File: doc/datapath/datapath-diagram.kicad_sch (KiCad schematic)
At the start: 26 parts, among them U17 ip, U19 insn, U27 stack[0], U28 stack[1], U29 ……, U32 cd_timer, U4 cstack[0], U5 cstack[1], U6 ……

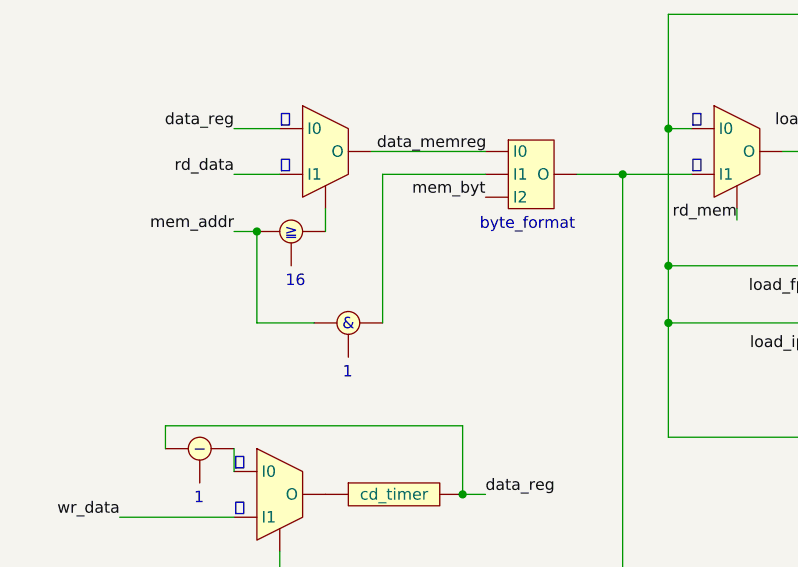
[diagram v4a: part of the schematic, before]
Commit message: CPUを新しいISAに合わせて再実装
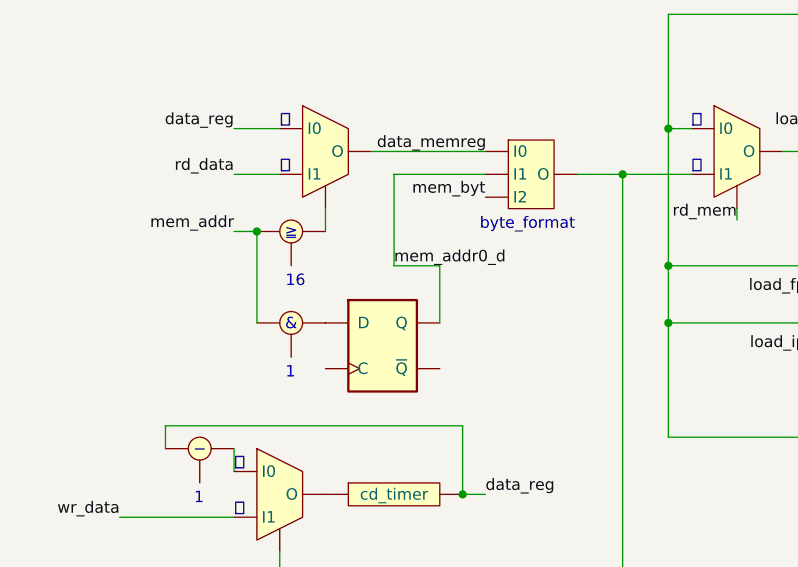
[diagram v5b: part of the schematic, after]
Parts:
- added U9: D-FF, symbol uchan:D-FF
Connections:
- net at U28.: now also U15. (O), U3. (O)
- net at U27.: now also U3. (O), U40. (O); no longer U18. (O)
- new net: U1., U31. (O)
- new net: U18. (O), U19., U34. (O)
- new net: U18. (O), U27.
- new net: U32., U36. (O)
- new net: U33., U9.~ (~{Q})
- new net: U., U40. (O)
- new net: U17., U40. (O)
- new net: U4., U40. (O)
- new net: U12. (O), U40. (O)
- new net: U36. (O), U37.
- new net: U12. (O), U2.
- new net: U15. (O), U2.
- new net: U36. (O), U39.
- new net: U38., U39.
- new net mem_addr0_d: U34. (O), U9.~ (~{Q})
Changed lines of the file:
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@@
-    (stroke (width 0) (type default))
-  )
-  (wire (pts (xy 111.76 69.85) (xy 111.76 53.34))
     (stroke (width 0) (type default))
   )
@@
     (stroke (width 0) (type default))
   )
-  (wire (pts (xy 97.79 69.85) (xy 104.14 69.85))
+  (wire (pts (xy 113.03 63.5) (xy 113.03 53.34))
     (stroke (width 0) (type default))
   )
@@
     (stroke (width 0) (type default))
   )
+  (wire (pts (xy 118.11 63.5) (xy 113.03 63.5))
+    (stroke (width 0) (type default))
+  )
   (wire (pts (xy 184.15 55.88) (xy 184.15 69.85))
     (stroke (width 0) (type default))
@@
     (stroke (width 0) (type default))
   )
+  (wire (pts (xy 118.11 69.85) (xy 118.11 63.5))
+    (stroke (width 0) (type default))
+  )
   (wire (pts (xy 186.69 58.42) (xy 193.04 58.42))
     (stroke (width 0) (type default))
@@
     (stroke (width 0) (type default))
   )
-  (wire (pts (xy 111.76 53.34) (xy 123.19 53.34))
+  (wire (pts (xy 113.03 53.34) (xy 123.19 53.34))
     (stroke (width 0) (type default))
   )
@@
   )
   (text_box "&"
-    (at 106.68 68.58 0) (size 2.54 2.54)
+    (at 100.33 68.58 0) (size 2.54 2.54)
     (stroke (width -0.0001) (type default))
     (fill (type none))
@@
     (effects (font (size 1.27 1.27)) (justify left bottom))
   )
-  (text "1" (at 107.315 76.2 0)
+  (text "1" (at 100.965 76.2 0)
     (effects (font (size 1.27 1.27)) (justify left bottom))
   )
@@
   )
   (label "load_fp" (at 191.77 124.46 0) (fields_autoplaced)
+    (effects (font (size 1.27 1.27)) (justify left bottom))
+  )
+  (label "mem_addr0_d" (at 113.03 63.5 0) (fields_autoplaced)
     (effects (font (size 1.27 1.27)) (justify left bottom))
   )
@@
     )
   )
-  (symbol (lib_id "Logic_Component:ALU_Circle_Left_Bottom") (at 107.95 69.85 0) (unit 1)
+  (symbol (lib_id "Logic_Component:ALU_Circle_Left_Bottom") (at 101.6 69.85 0) (unit 1)
     (in_bom yes) (on_board yes) (dnp no) (fields_autoplaced)
-    (property "Reference" "U33" (at 107.95 67.31 0)
-      (effects (font (size 1.27 1.27)) hide)
-    )
-    (property "Value" "~" (at 107.95 69.85 0)
-      (effects (font (size 1.27 1.27)))
-    )
-    (property "Footprint" "" (at 107.95 69.85 0)
-      (effects (font (size 1.27 1.27)) hide)
-    )
-    (property "Datasheet" "" (at 107.95 69.85 0)
+    (property "Reference" "U33" (at 101.6 67.31 0)
+      (effects (font (size 1.27 1.27)) hide)
+    )
+    (property "Value" "~" (at 101.6 69.85 0)
+      (effects (font (size 1.27 1.27)))
+    )
+    (property "Footprint" "" (at 101.6 69.85 0)
+      (effects (font (size 1.27 1.27)) hide)
+    )
+    (property "Datasheet" "" (at 101.6 69.85 0)
       (effects (font (size 1.27 1.27)) hide)
     )
@@
         )
       )
+    )
+  )
+  (symbol (lib_id "uchan:D-FF") (at 111.76 72.39 0) (unit 1)
+    (in_bom yes) (on_board yes) (dnp no) (fields_autoplaced)
+    (property "Reference" "U9" (at 111.76 66.04 0)
+      (effects (font (size 1.27 1.27)) hide)
+    )
+    (property "Value" "D-FF" (at 111.76 66.2211 0)
+      (effects (font (size 1.27 1.27)) hide)
+    )
+    (property "Footprint" "" (at 111.76 72.39 0)
+      (effects (font (size 1.27 1.27)) hide)
+    )
+    (property "Datasheet" "74xx/74hc_hct74.pdf" (at 111.76 72.39 0)
+      (effects (font (size 1.27 1.27)) hide)
+    )
+    (pin "~")
+    (pin "~")
+    (pin "~")
+    (pin "~")
+    (instances
+      (project "datapath-diagram"
+        (path "/af1fd5ae-daa0-4a17-8ab4-fe581cd231ee"
+          (reference "U9") (unit 1)
+        )
+      )

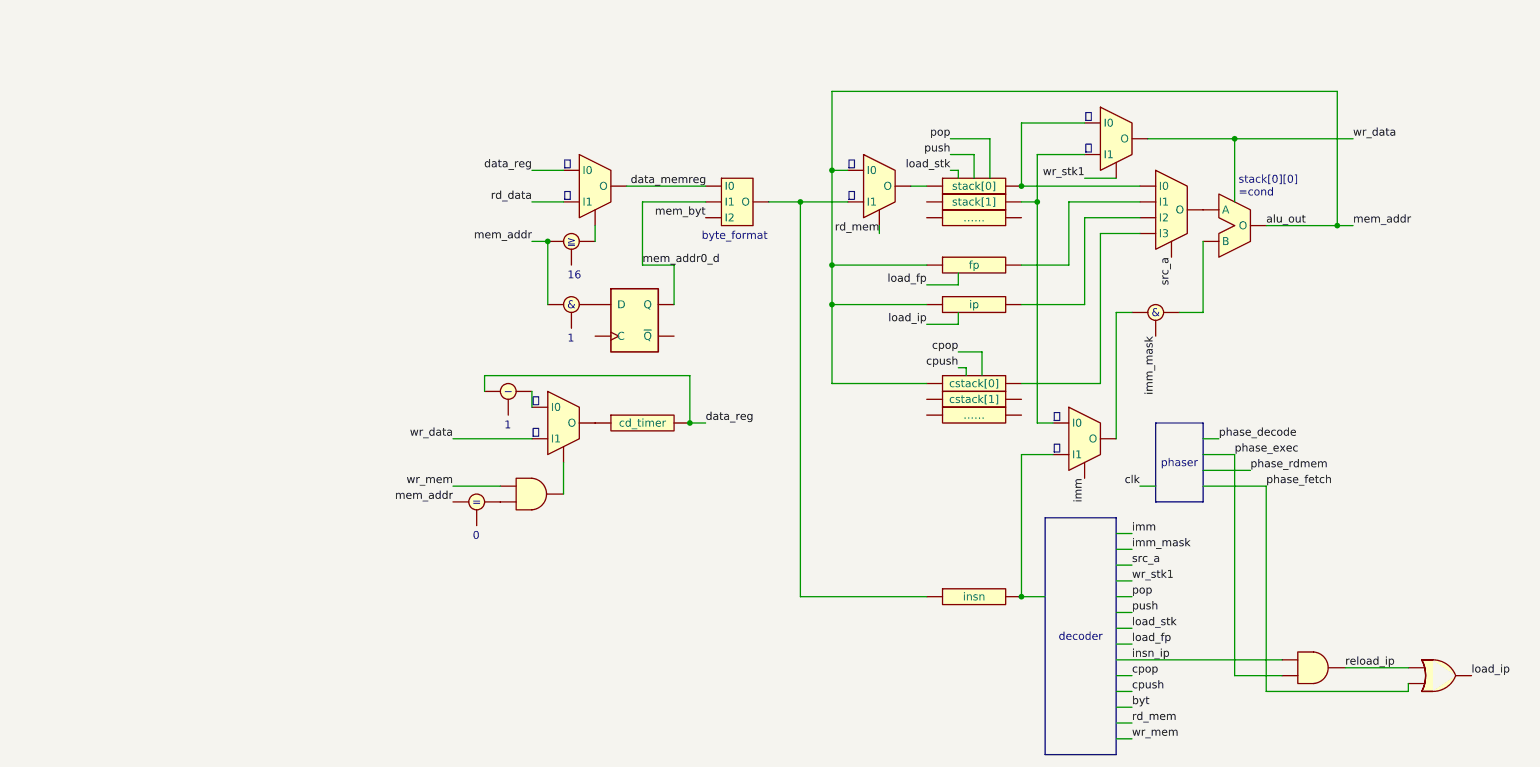
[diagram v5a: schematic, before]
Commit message: コードコメントとデータパス図を修正
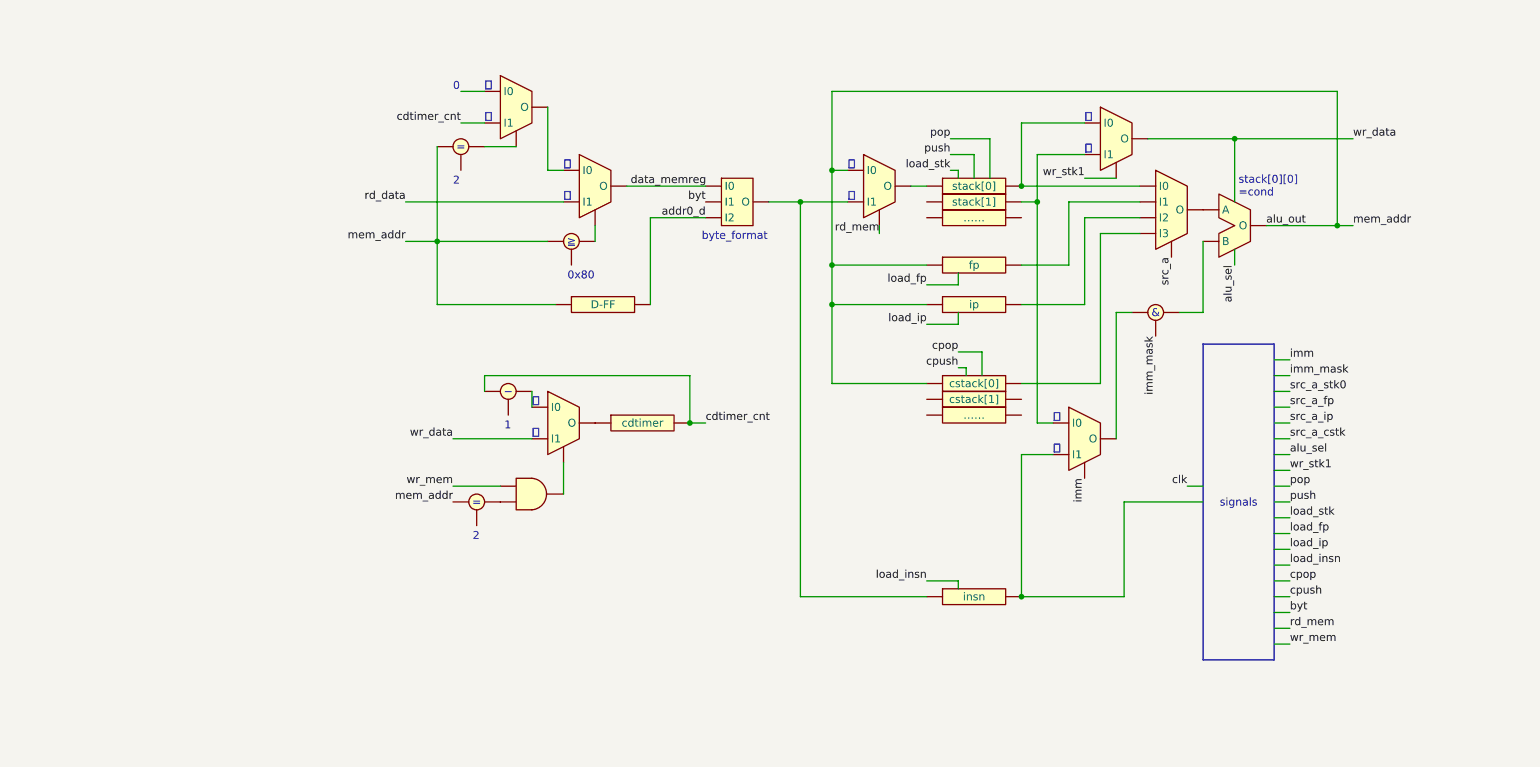
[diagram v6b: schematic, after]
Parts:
- removed U33: ~, symbol Logic_Component:ALU_Circle_Left_Bottom
- removed U7: ~, symbol Logic_Component:Gate_AND_2Input
- removed U8: ~, symbol Logic_Component:Gate_OR_2Input
- removed U9: D-FF, symbol uchan:D-FF
- added U7: ~, symbol Logic_Component:Multiplexer_2
- added U8: ~, symbol Logic_Component:ALU_Circle_Left_Bottom
- added U9: D-FF, symbol Logic_Component:Register_Simple_Normal
- U32: value cd_timer -> cdtimer
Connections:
- net mem_addr0_d is gone; now on net data_memreg: U34. (O)
- net mem_byt is gone; now on net data_memreg: U34. (O)
- net alu_out: now also U8., U9.
- net byt: now also U34. (O)
- net at U28.: now also U15. (O), U3. (O)
- net at U27.: now also U3. (O), U40. (O); no longer U18. (O)
- net cdtimer_cnt: now reaches U32.
- net cdtimer_cnt: now also U37., U7. (O); no longer U36. (O)
- removed net data_reg: U31. (O), U32., U37.
- new net: U31. (O), U7. (O)
- new net: U1., U31. (O)
- new net: U18. (O), U19., U34. (O)
- new net: U18. (O), U27.
- new net: U32., U36. (O)
- new net: U., U40. (O)
- new net: U7. (O), U8.
- new net: U17., U40. (O)
- new net: U4., U40. (O)
- new net: U12. (O), U40. (O)
- new net: U36. (O), U37.
- new net: U12. (O), U2.
- new net: U15. (O), U2.
- new net: U36. (O), U39.
- new net: U38., U39.
- new net addr0_d: U34. (O), U9.
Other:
- note added: "0x80"
- note added: "2"
- note removed: "16"

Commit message: データパス図を現状に合わせて更新
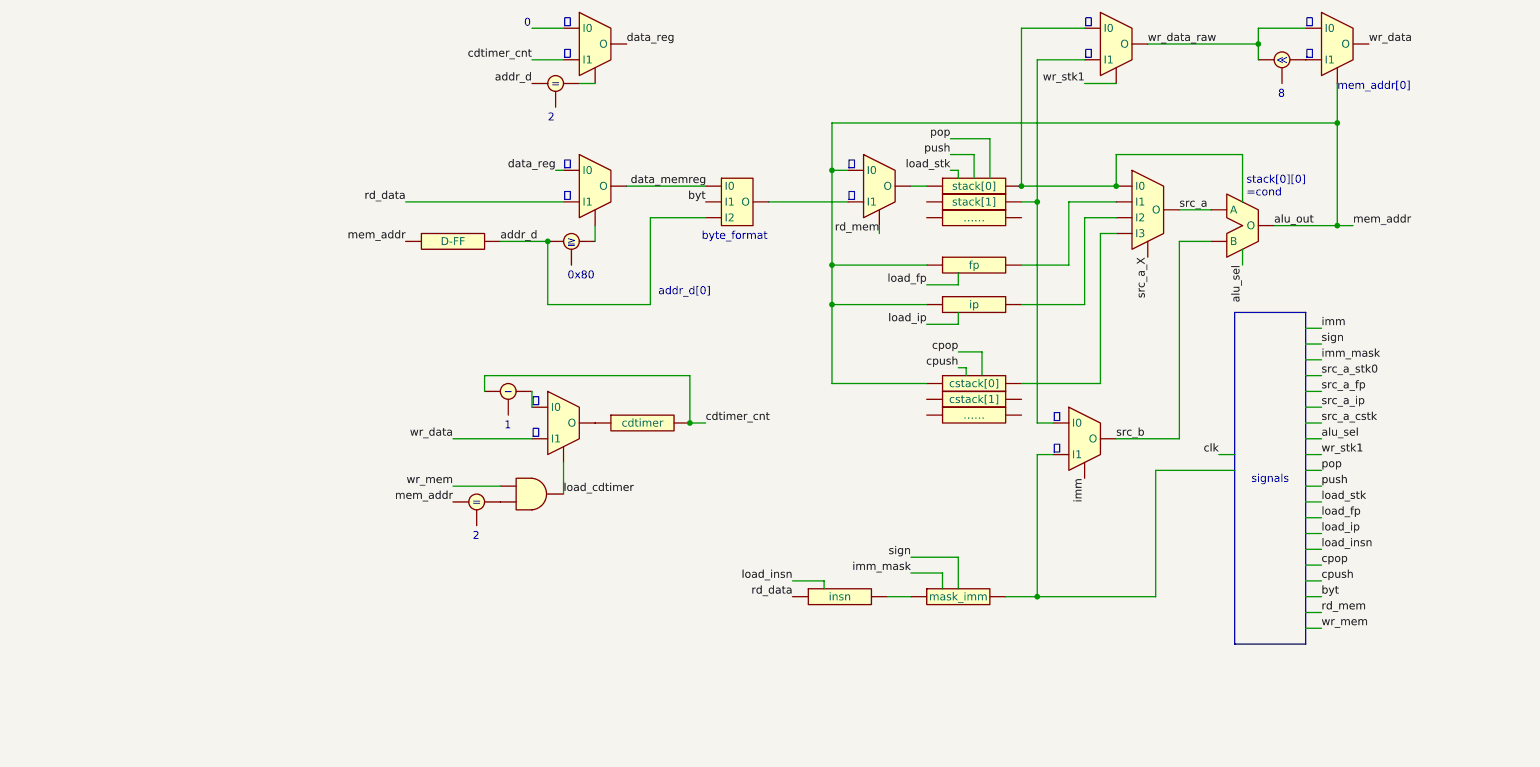
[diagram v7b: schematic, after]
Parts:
- removed U2: ~, symbol Logic_Component:ALU_Circle_Left_Bottom
- added U10: ~, symbol Logic_Component:Multiplexer_2
- added U11: ~, symbol Logic_Component:ALU_Circle_Left_Bottom
- added U13: mask_imm, symbol Logic_Component:Register_Simple_Normal
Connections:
- net alu_out: now also U10. (O); no longer U1., U8.
- net rd_data: now also U19.
- net src_a: now also U12. (O)
- net wr_data: now also U10. (O); no longer U3. (O)
- net at U28.: now also U15. (O), U3. (O)
- net data_reg: now reaches U31. (O), U7. (O)
- net addr_d: now reaches U1.
- net addr_d: now also U34. (O), U8., U9.; no longer U31. (O)
- net at U27.: now also U3. (O), U40. (O); no longer U18. (O)
- net src_a_X: now reaches U40. (O)
- net src_a_X: no longer U.
- net src_b: now reaches U12. (O)
- net src_b: now also U15. (O); no longer U40. (O)
- removed net addr0_d: U34. (O), U9.
- new net: U1., U31. (O)
- new net: U10. (O), U11.
- new net: U18. (O), U34. (O)
- new net: U18. (O), U27.
- new net: U32., U36. (O)
- new net: U., U40. (O)
- new net: U7. (O), U8.
- new net: U17., U40. (O)
- new net: U4., U40. (O)
- new net: U36. (O), U37.
- new net: U13., U19.
- new net: U13., U15. (O)
- new net: U38., U39.
- new net load_cdtimer: U36. (O), U39.
- new net wr_data_raw: U10. (O), U11., U3. (O)
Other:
- note added: "8"
- note added: "addr_d[0]"
- note added: "mem_addr[0]"
